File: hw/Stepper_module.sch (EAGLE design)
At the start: 43 parts, among them J1 GROVE-4P-2.0-3470130P1, J2 GROVE-4P-2.0-3470130P1, X1 22-23-2021, X2 22-23-2041, X4 53047-04, X5 53047-04

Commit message: Added bottom silkscreen
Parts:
- SOT1: device maxim:MAX3051EKA -> r2p_ic:MAX3051EKA
- U$3: device maxim:MAX17501 -> r2p_ic:MAX17501
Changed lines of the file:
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@@
 <part name="GND2" library="supply" deviceset="GND" device=""/>
 <part name="GND3" library="supply" deviceset="GND" device=""/>
-<part name="U$3" library="maxim" deviceset="MAX17501" device=""/>
+<part name="U$3" library="r2p_ic" deviceset="MAX17501" device=""/>
 <part name="J1" library="OPL Eagle Library" deviceset="GROVE-4P-2.0" device="-3470130P1"/>
 <part name="+3V7" library="supply1" deviceset="+3V3" device=""/>
@@
 <part name="FRAME1" library="frames" deviceset="DINA3_L" device=""/>
 <part name="GND13" library="supply" deviceset="GND" device=""/>
-<part name="SOT1" library="maxim" deviceset="MAX3051" device="EKA"/>
+<part name="SOT1" library="r2p_ic" deviceset="MAX3051" device="EKA"/>
 <part name="U$1" library="r2p_pcb" deviceset="PCB_25X45" device=""/>
 <part name="U$5" library="abracon" deviceset="ASD" device=""/>

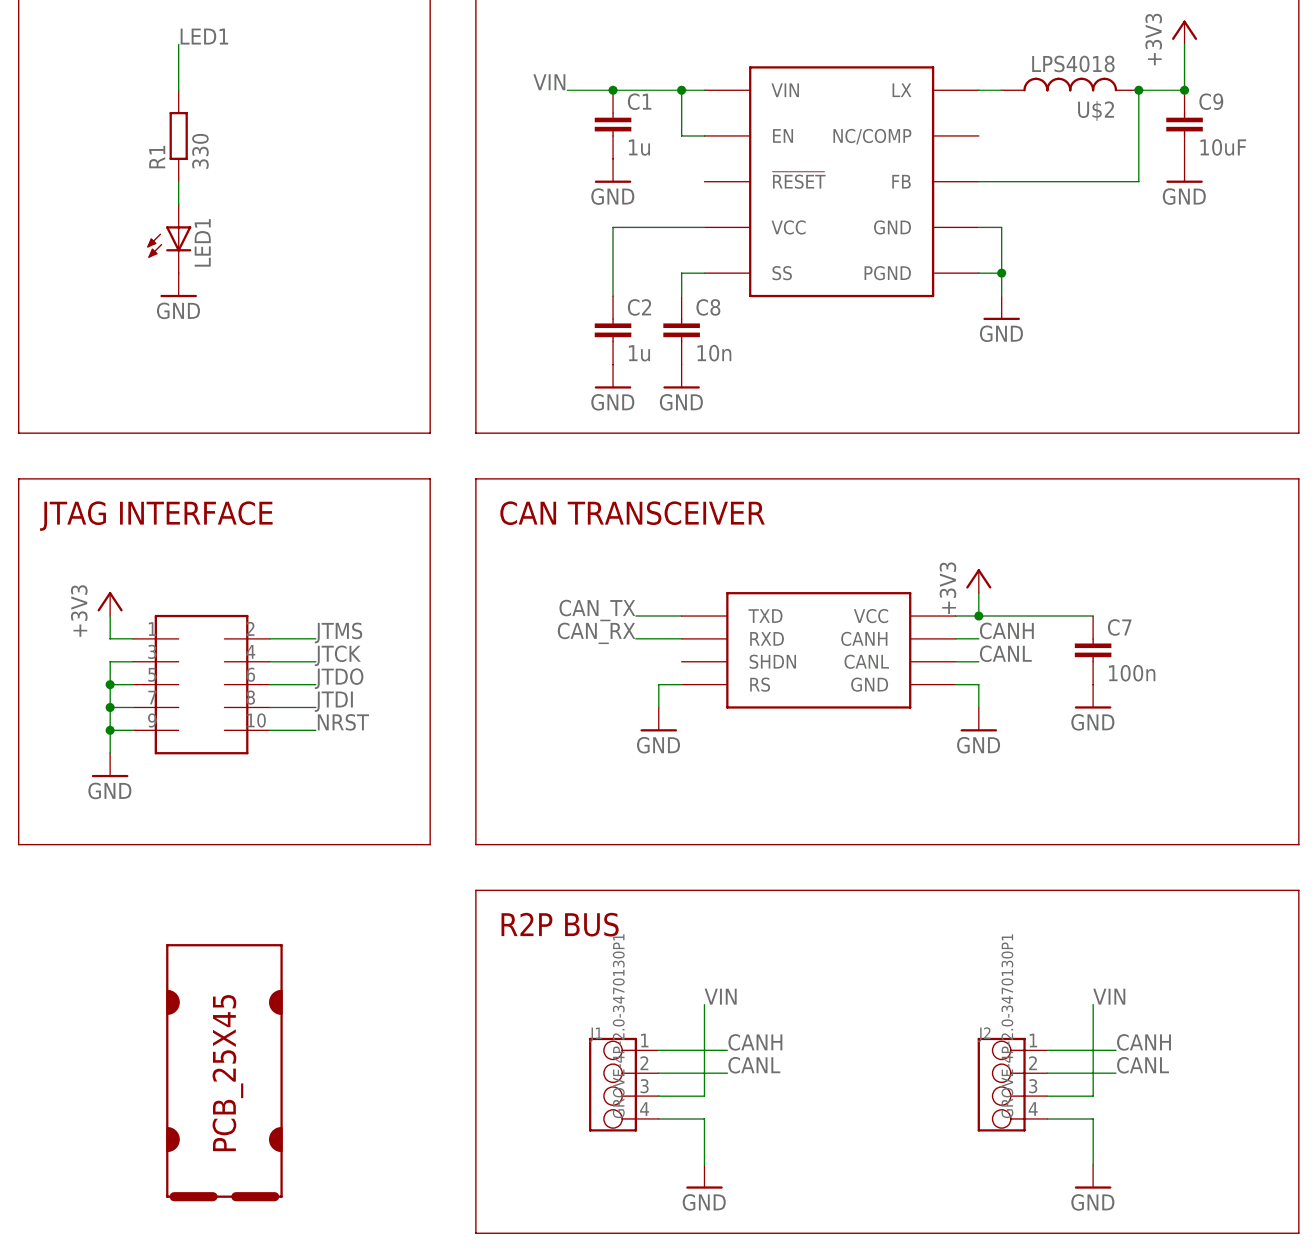
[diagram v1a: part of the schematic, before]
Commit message: Updated components to R2P Eagle libraries
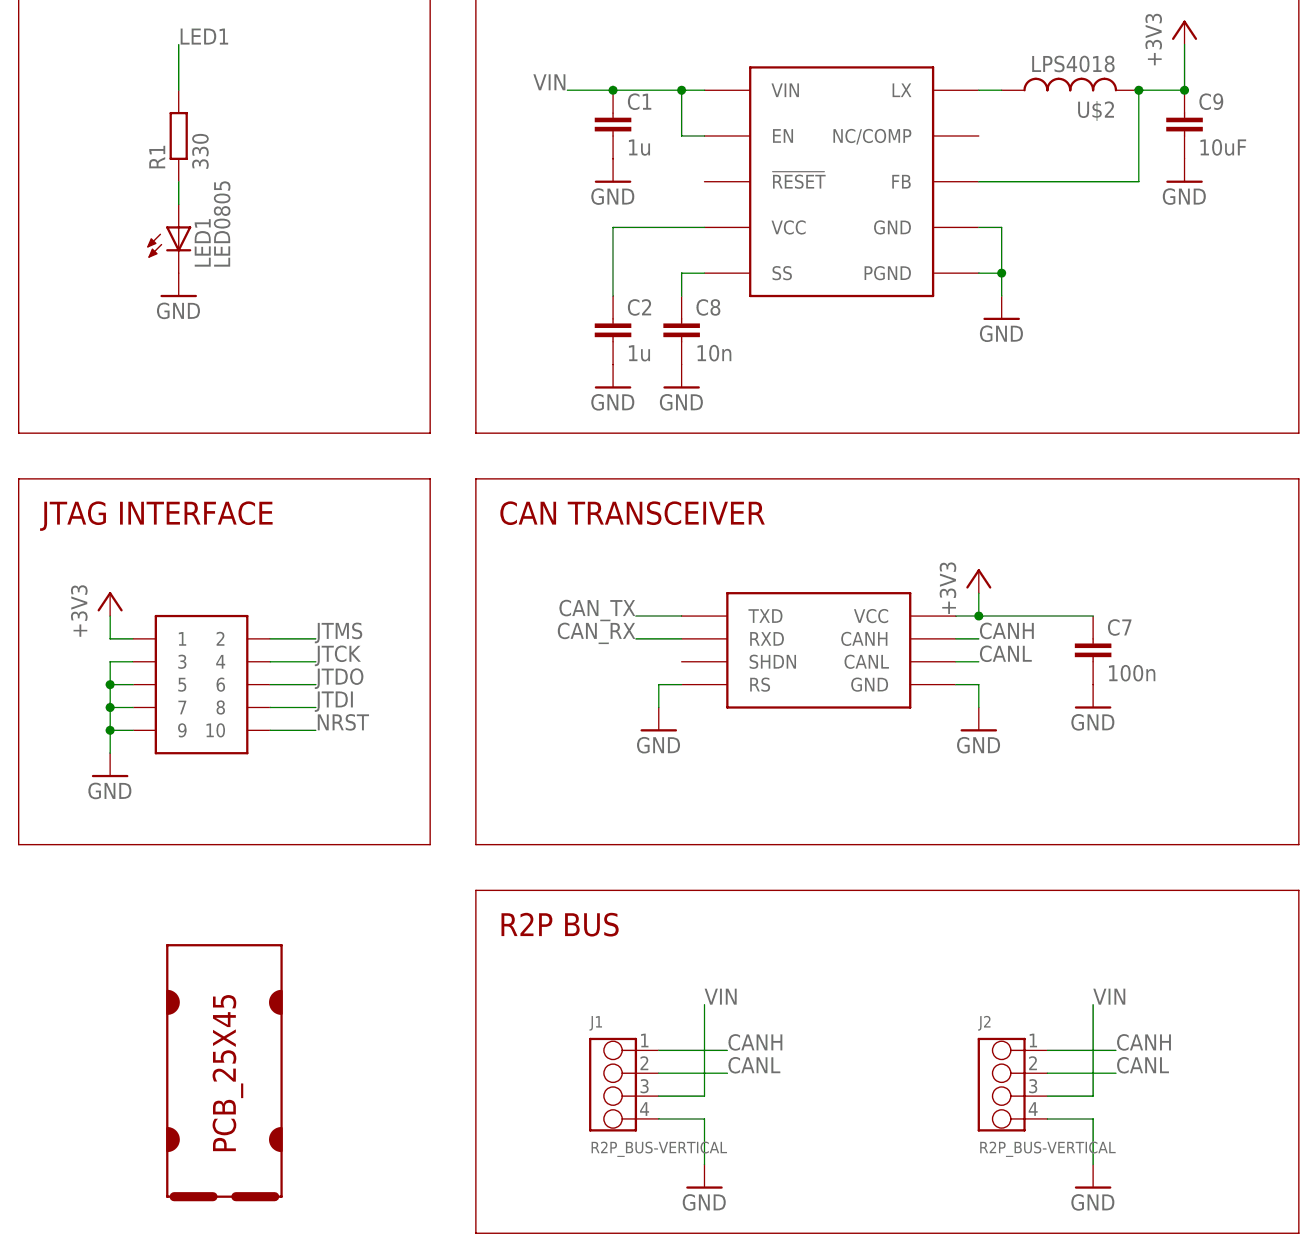
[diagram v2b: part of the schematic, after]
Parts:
- C1: device rcl:C-EUC1206 -> r2p_rcl:C1206
- C11, C12, C13, C14, C16, C17, C18, C19, C2, C20, C3, C4, C6, C7, C8: device rcl:C-EUC0603 -> r2p_rcl:C0603
- C15, C5, C9: device rcl:C-EUC0805 -> r2p_rcl:C0805
- J1, J2: value GROVE-4P-2.0-3470130P1 -> R2P_BUS-VERTICAL; device OPL Eagle Library:GROVE-4P-2.0-3470130P1 -> r2p_connector:R2P_BUS-VERTICAL
- LED1: value (none) -> LED0805; device led:LEDCHIPLED_0805 -> r2p_led:LED0805
- R1, R2, R3, R4, R5: device rcl:R-EU_R0603 -> r2p_rcl:R0603
- U$4: value FTSH-105TH -> JTAG-TH; device samtec:FTSH-105TH -> r2p_connector:JTAG-TH
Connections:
- net +3V3: now also U$4.1; no longer U$4.P$1
- net GND: now also U$4.3, U$4.5, U$4.7, U$4.9; no longer U$4.P$3, U$4.P$5, U$4.P$7, U$4.P$9
- net JTCK: now also U$4.4; no longer U$4.P$4
- net JTDI: now also U$4.8; no longer U$4.P$8
- net JTDO: now also U$4.6; no longer U$4.P$6
- net JTMS: now also U$4.2; no longer U$4.P$2
- net NRST: now also U$4.10; no longer U$4.P$10
